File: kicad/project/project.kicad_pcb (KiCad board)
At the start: 2 copper layers, 98 x 60 mm, 42 parts, among them J1 SWD, J3 Voltmeter, U1 ADS1015, U2 AP7380, U3 STM32L031F4Px, U4 VN7003ALH

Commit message: Tidying
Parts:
- moved TP1 3.65 mm to (120.5, 124.0)
- moved R13 2.31 mm to (137.5, 124.0)
- moved R16 1.63 mm to (136.5, 121.0), turned to 0 degrees
- moved R12 1.32 mm to (137.5, 126.0)
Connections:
- C2 pad 2: Earth -> GND
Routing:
- net Net-(R13-Pad1): track 35.9 -> 31.7 mm
- net CURRENT_SENSE: track 66.6 -> 62.7 mm
- net /AIN3: track 7.53 -> 4.29 mm
- net GND: track 347.6 -> 349.3 mm, vias 11 -> 12
- net /FR_DIAG: track 38.1 -> 36.7 mm
- net Net-(R12-Pad2): track 30.0 -> 29.0 mm
- net +3V3: track 121.0 -> 120.2 mm
- net /INPUT: track 30.6 -> 29.9 mm
- net SCL: track 62.8 -> 62.3 mm

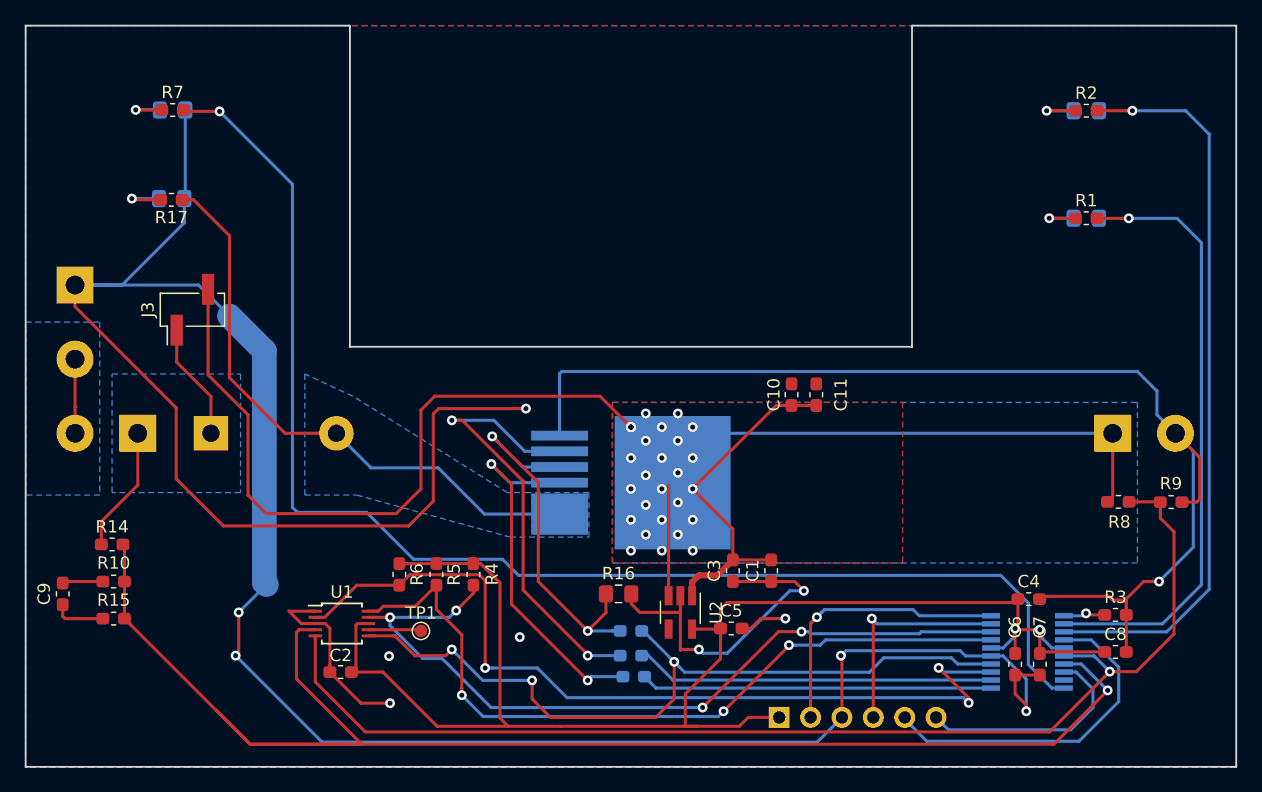
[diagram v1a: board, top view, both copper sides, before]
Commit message: Changed diode footprint
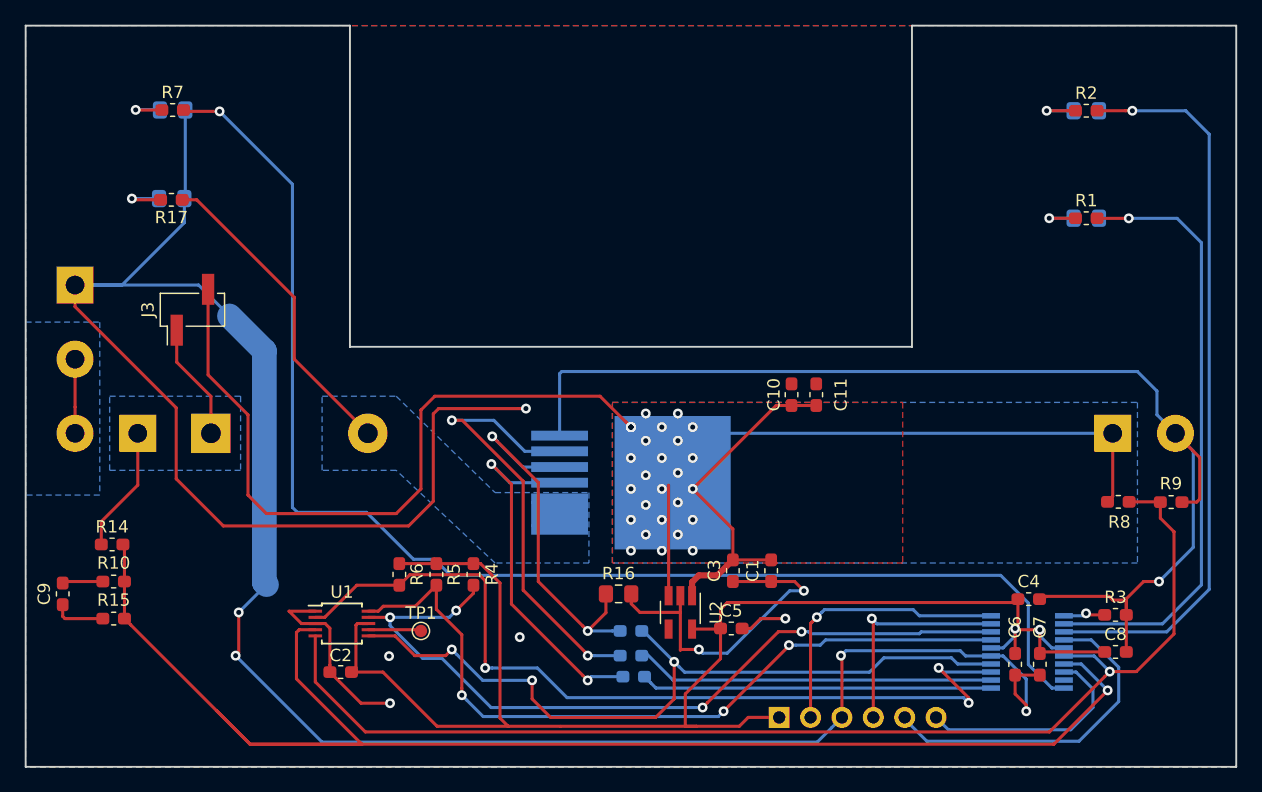
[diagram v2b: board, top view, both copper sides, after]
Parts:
- D5: footprint Diode_THT:D_5KP_P10.16mm_Horizontal -> Diode_THT:D_DO-201AD_P12.70mm_Horizontal
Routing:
- net /LED_4: track 47.8 -> 25.8 mm

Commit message: Grounds
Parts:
- moved R1 8.68 mm to (174.4, 81.9), turned to 180 degrees
- moved D1 8.59 mm to (174.5, 82.0), turned to 0 degrees
- moved D2 7.11 mm to (174.5, 89.0), turned to 0 degrees
- moved R2 6.97 mm to (174.4, 88.9), turned to 180 degrees
- moved TP1 1.17 mm to (121.5, 124.6)
- moved R17 0.25 mm to (100.5, 88.9), turned to 0 degrees
- moved D3 0.10 mm to (100.3, 81.9), turned to 0 degrees
- moved R7 0.10 mm to (100.3, 81.9), turned to 180 degrees
- moved D4 0.10 mm to (100.4, 89.0), turned to 0 degrees
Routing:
- net GND: track 349.3 -> 263.4 mm, vias 12 -> 14
- net +24V: track 138.4 -> 155.3 mm, vias 27 -> 30
- net /LED_4: track 25.8 -> 39.5 mm
- net /LED_2: track 59.9 -> 47.4 mm
- net /LED_3: track 108.9 -> 120.3 mm, vias 1 -> 3
- net /FR_DIAG: track 36.7 -> 33.6 mm
- net SDA: track 64.7 -> 62.5 mm, vias 4 -> 5
- net /LED_1: track 49.4 -> 51.5 mm
- net Net-(R3-Pad1): track 3.43 -> 4.72 mm
- net /AIN3: track 4.29 -> 5.54 mm
- net /PANEL_SENSE: track 96.1 -> 97.1 mm
- net SCL: track 62.3 -> 63.0 mm

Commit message: SWD header
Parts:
- moved J1 12.0 mm to (161.5, 130.6), turned to 90 degrees
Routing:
- net GND: track 263.4 -> 217.5 mm
- net UART_TX: track 18.3 -> 33.6 mm
- net NRST: track 27.7 -> 36.7 mm, vias 0 -> 2
- net SWCLK: track 22.9 -> 15.9 mm
- net SWDI0: track 17.9 -> 20.5 mm
- net +3V3: track 120.7 -> 120.1 mm

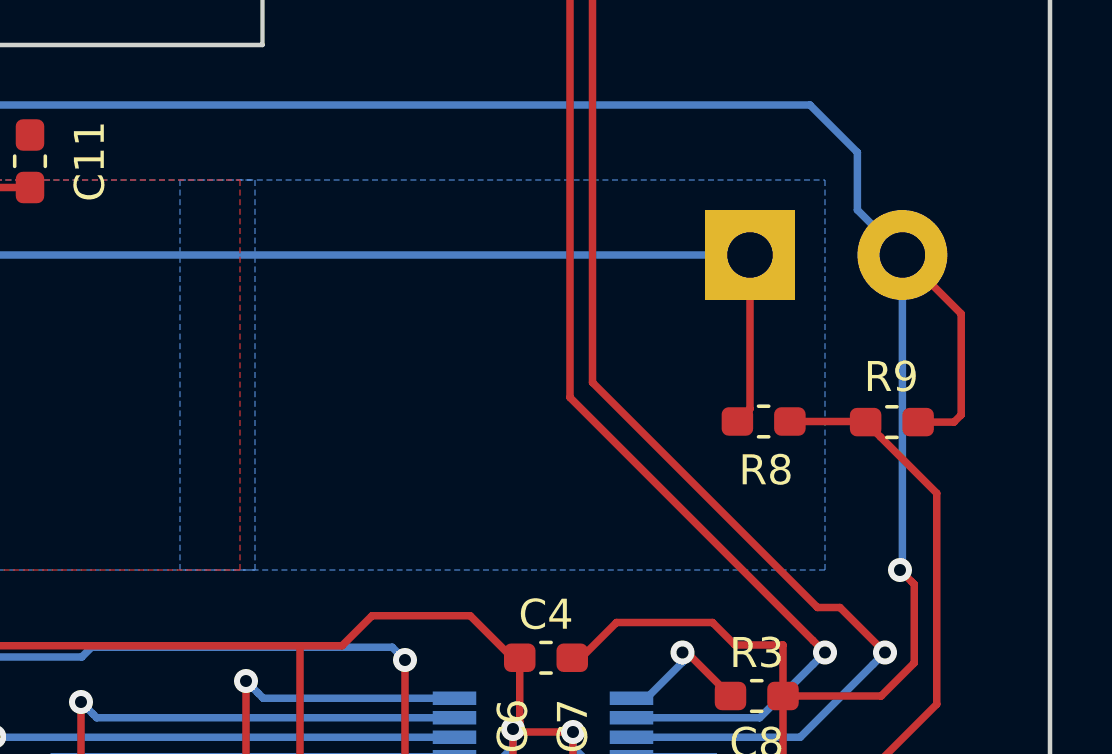
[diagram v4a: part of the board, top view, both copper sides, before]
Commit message: Input copper pour re-shape
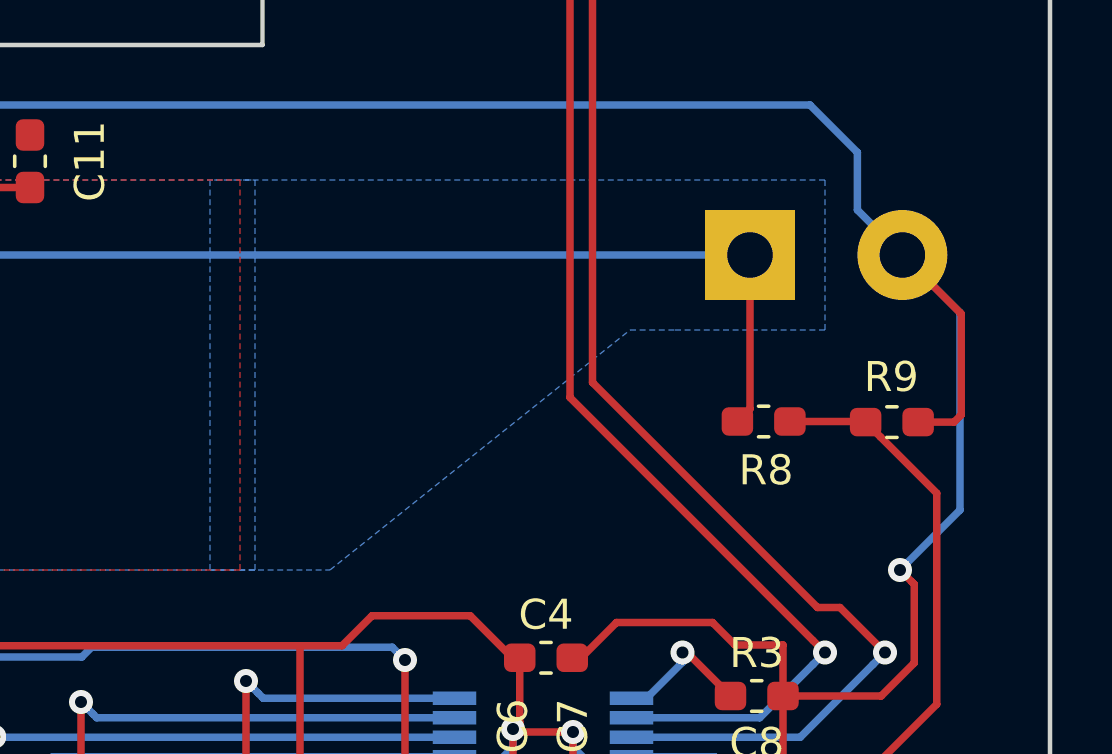
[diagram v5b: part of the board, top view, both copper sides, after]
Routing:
- net GND: track 217.5 -> 219.1 mm
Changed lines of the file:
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@@
     (thickness 1.6)
     (drawings 25)
-    (tracks 479)
+    (tracks 480)
     (zones 0)
     (modules 42)
@@
   (segment (start 182.105 113.57) (end 183.3 113.57) (width 0.25) (layer F.Cu) (net 2))
   (via (at 181.5 118.5) (size 0.8) (drill 0.4) (layers F.Cu B.Cu) (net 2))
-  (segment (start 181.58 118.42) (end 181.5 118.5) (width 0.25) (layer B.Cu) (net 2))
-  (segment (start 181.58 108) (end 181.58 118.42) (width 0.25) (layer B.Cu) (net 2))
   (segment (start 181.899999 118.899999) (end 181.5 118.5) (width 0.25) (layer F.Cu) (net 2))
   (segment (start 181.975001 121.598001) (end 181.975001 118.975001) (width 0.25) (layer F.Cu) (net 2))
@@
   (segment (start 141.5 124.965685) (end 142.734315 126.2) (width 0.25) (layer F.Cu) (net 2))
   (segment (start 142.734315 126.2) (end 143.3 126.2) (width 0.25) (layer F.Cu) (net 2))
+  (segment (start 183.5 116.5) (end 181.5 118.5) (width 0.25) (layer B.Cu) (net 2))
+  (segment (start 183.5 109.92) (end 183.5 116.5) (width 0.25) (layer B.Cu) (net 2))
+  (segment (start 181.58 108) (end 183.5 109.92) (width 0.25) (layer B.Cu) (net 2))
   (via (at 141.3 113.6) (size 0.8) (drill 0.4) (layers F.Cu B.Cu) (net 3))
   (via (at 141.3 111.2) (size 0.8) (drill 0.4) (layers F.Cu B.Cu) (net 3))
@@
     )
   )
-  (zone (net 3) (net_name +24V) (layer B.Cu) (hatch edge 0.508)
-    (priority 10)
-    (connect_pads yes (clearance 0.508))
-    (min_thickness 0.254)
-    (fill yes (arc_segments 16) (thermal_gap 0.508) (thermal_bridge_width 0.508) (smoothing fillet) (radius 1))
-    (polygon
-      (pts
-        (xy 157.5 105.5) (xy 179 105.5) (xy 179 118.5) (xy 157.5 118.5)
-      )
-    )
-  )
   (zone (net 0) (net_name "") (layer B.Mask) (hatch full 0.508)
     (priority 10)
@@
     (polygon
       (pts
-        (xy 136 105.5) (xy 179 105.5) (xy 179 118.5) (xy 136 118.5)
+        (xy 136 105.5) (xy 159.5 105.5) (xy 159.5 118.5) (xy 136 118.5)
       )
     )
@@
       )
     )
+  )
+  (zone (net 3) (net_name +24V) (layer B.Cu) (hatch edge 0.508)
+    (priority 10)
+    (connect_pads yes (clearance 0.508))
+    (min_thickness 0.254)
+    (fill yes (arc_segments 16) (thermal_gap 0.508) (thermal_bridge_width 0.508) (smoothing fillet) (radius 2))
+    (polygon
+      (pts
+        (xy 179 105.5) (xy 158.5 105.5) (xy 158.5 118.5) (xy 162.5 118.5) (xy 172.5 110.5)
+        (xy 174 110.5) (xy 179 110.5)
+      )
+    )
+  )
+  (zone (net 0) (net_name "") (layer B.Mask) (hatch full 0.508)
+    (priority 10)
+    (connect_pads yes (clearance 0.508))
+    (min_thickness 0.254)
+    (fill yes (arc_segments 16) (thermal_gap 0.508) (thermal_bridge_width 0.508) (smoothing fillet) (radius 1))
+    (polygon
+      (pts
+        (xy 155.5 105.5) (xy 155.5 118.5) (xy 162.5 118.5) (xy 172.5 110.5) (xy 174.5 110.5)
+        (xy 174.5 105.5)
+      )
+    )

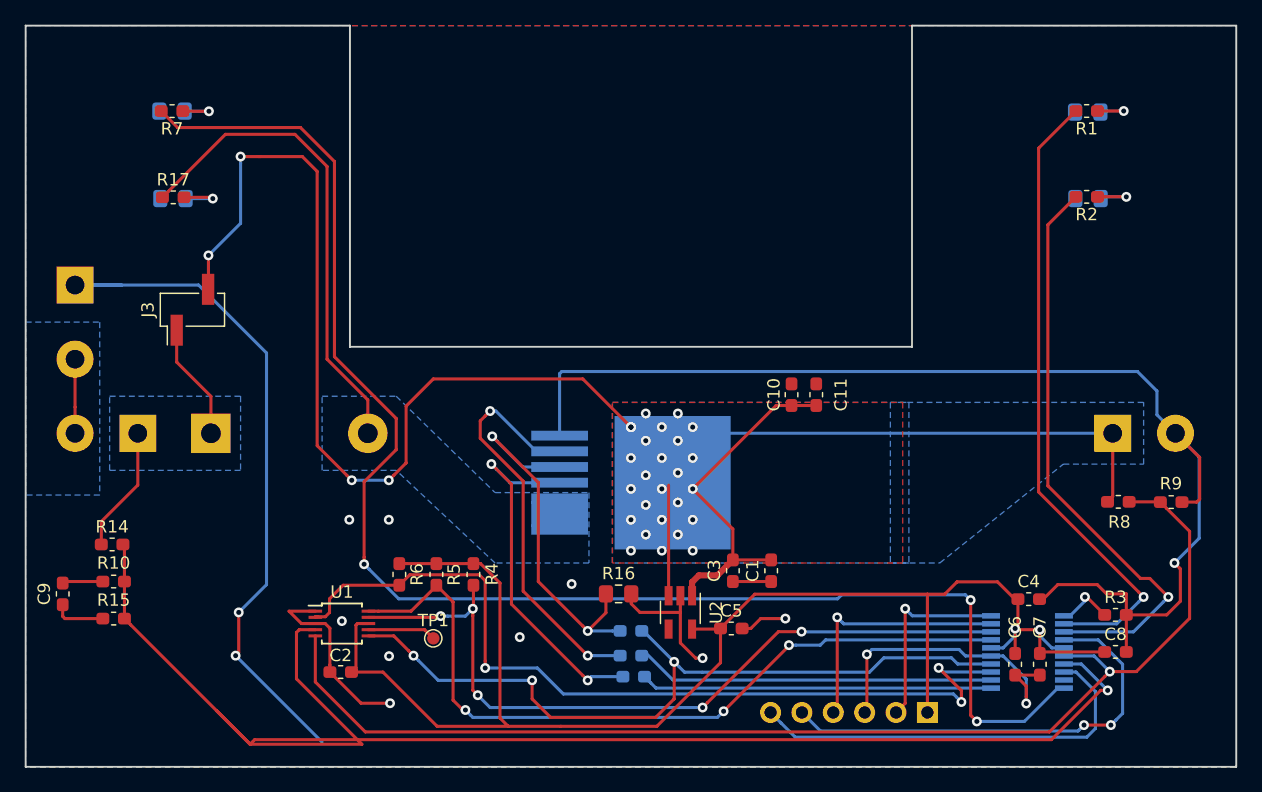
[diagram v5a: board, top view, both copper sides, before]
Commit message: Sense battery before the diode
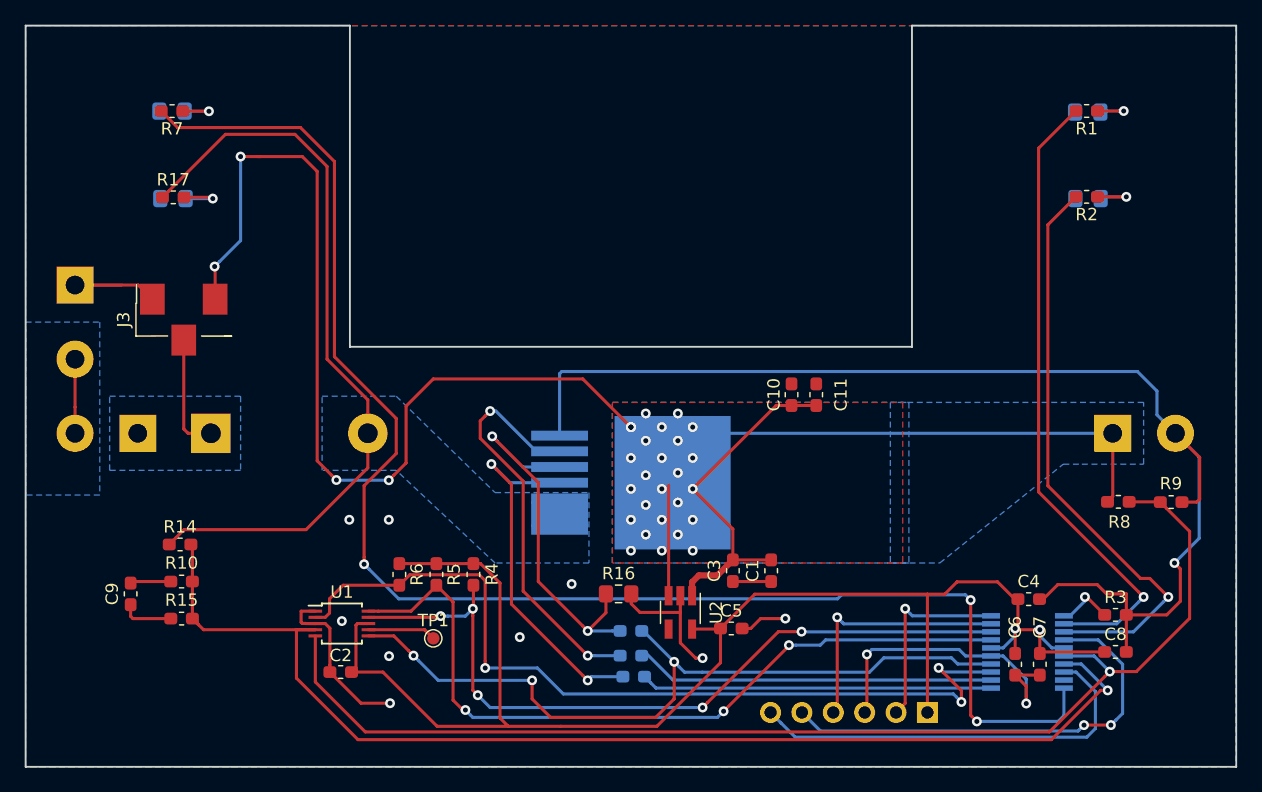
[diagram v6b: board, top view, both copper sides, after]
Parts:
- J3: footprint Connector_PinHeader_2.54mm:PinHeader_1x02_P2.54mm_Vertical_SMD_Pin1Left -> theapi:Header_1x03_SMD_Pin1Right
- moved C9 5.50 mm to (97.0, 121.0)
- moved R10 5.50 mm to (101.1, 120.0)
- moved R14 5.50 mm to (101.0, 117.0)
- moved R15 5.50 mm to (101.1, 123.0)
- moved J3 1.06 mm to (101.3, 98.8)
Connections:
- BT1 pad 1: /BATT -> /DIODE
- D4 pad 2: Net-(D4-Pad2) -> /LED_4
- D5 pad 1: /BATT -> /DIODE
- D5 pad 2: /LED_4 -> /OUT
- J3 pad 1: /BATT -> GND
- J3 pad 2: +24V -> /DIODE
- R14 pad 1: /BATT -> /OUT
- R17 pad 1: /LED_4 -> /OUT
- R17 pad 2: Net-(D4-Pad2) -> /LED_4
- U4 pad 1: /LED_4 -> /OUT
- U4 pad 2: /LED_4 -> /OUT
- U4 pad 3: /LED_4 -> /OUT
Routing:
- net /OUT: track 0.00 -> 60.9 mm
- net GND: track 219.1 -> 171.4 mm, vias 14 -> 12
- net /LED_4: track 39.5 -> 4.57 mm, vias 0 -> 1
- net /BATT_SENSE: track 121.8 -> 96.4 mm
- net /BATT: track 19.7 -> 0.00 mm
- net /DIODE: track 0.00 -> 9.54 mm
- net Net-(D4-Pad2): track 4.57 -> 0.00 mm, vias 1 -> 0
- net +24V: track 155.3 -> 156.6 mm
- net /LED_3: track 120.2 -> 121.5 mm
- added copper zone on B.Cu, net /DIODE
- added copper zone on B.Cu, net /OUT
- removed copper zone on B.Cu, net /BATT
- removed copper zone on B.Cu, net /LED_4
